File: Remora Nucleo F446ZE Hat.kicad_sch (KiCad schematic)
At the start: 5 parts, among them J1 NucleoF446ZE CN11 Header, J2 NucleoF446ZE CN12 Header

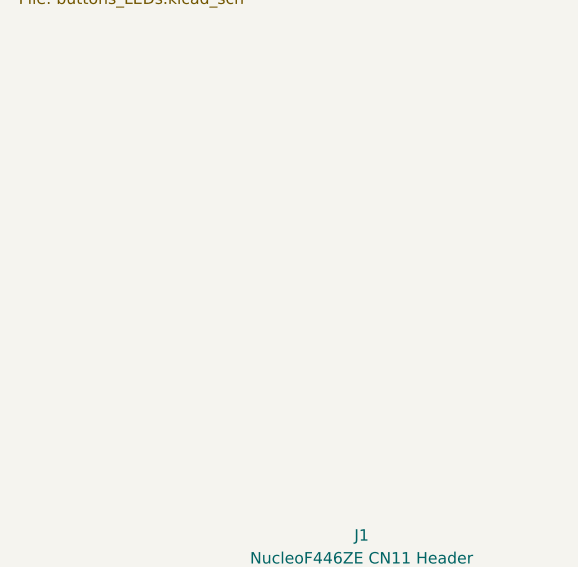
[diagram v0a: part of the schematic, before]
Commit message: tidy of some sheets. Added 0-10V DAC, but untested - only some basic validation on simulator for now
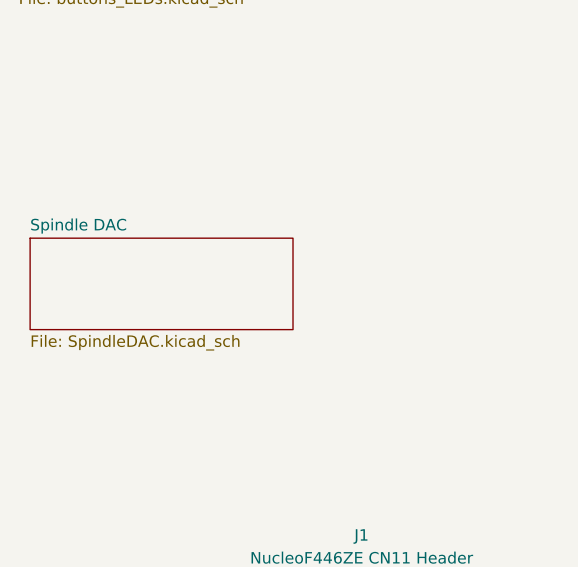
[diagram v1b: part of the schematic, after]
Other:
- added sheet Spindle DAC (SpindleDAC.kicad_sch)
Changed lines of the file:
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@@
+	)
+	(sheet
+		(at 16.51 71.12)
+		(size 29.21 10.16)
+		(exclude_from_sim no)
+		(in_bom yes)
+		(on_board yes)
+		(dnp no)
+		(fields_autoplaced yes)
+		(stroke
+			(width 0.1524)
+			(type solid)
+		)
+		(fill
+			(color 0 0 0 0.0000)
+		)
+		(property "Sheetname" "Spindle DAC"
+			(at 16.51 70.4084 0)
+			(effects
+				(font
+					(size 1.27 1.27)
+				)
+				(justify left bottom)
+			)
+		)
+		(property "Sheetfile" "SpindleDAC.kicad_sch"
+			(at 16.51 81.8646 0)
+			(effects
+				(font
+					(size 1.27 1.27)
+				)
+				(justify left top)
+			)
+		)
+		(instances
+			(project "Remora Nucleo F446ZE Hat"
+				(path "/5473abc6-7b93-43cc-a401-f691c4d7d7cf"
+					(page "18")
+				)
+			)
+		)
 	)
 	(sheet

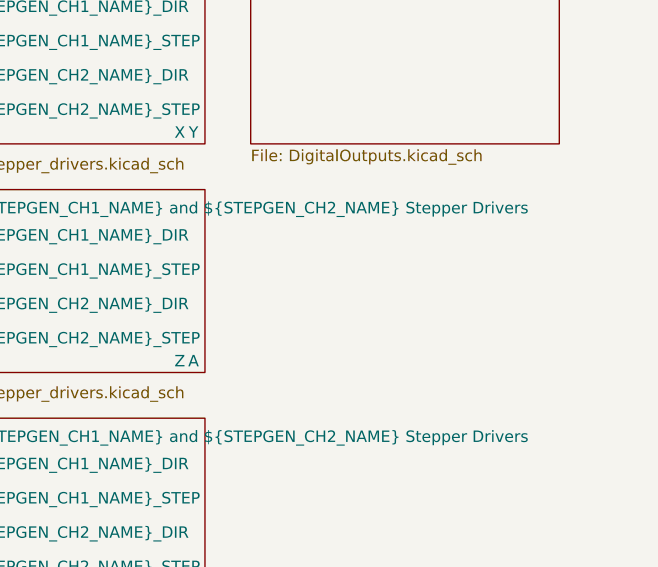
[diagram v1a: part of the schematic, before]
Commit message: digital inputs section
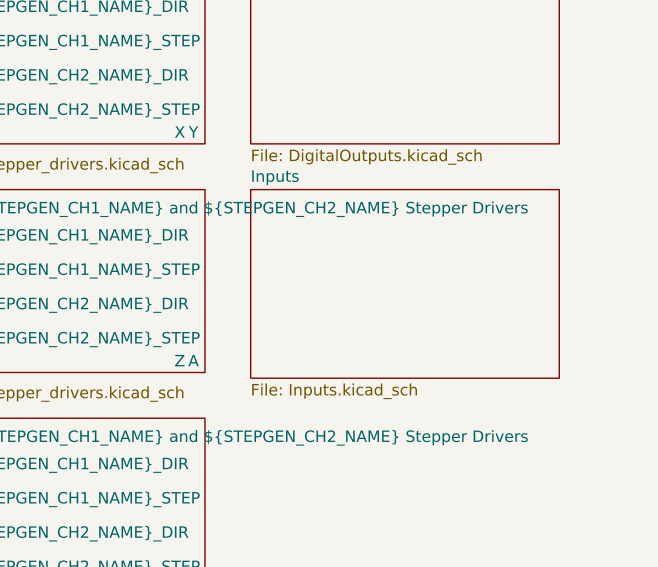
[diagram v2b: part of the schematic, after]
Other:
- added sheet Inputs (Inputs.kicad_sch)
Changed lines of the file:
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@@
+	)
+	(sheet
+		(at 246.38 41.91)
+		(size 34.29 20.955)
+		(exclude_from_sim no)
+		(in_bom yes)
+		(on_board yes)
+		(dnp no)
+		(fields_autoplaced yes)
+		(stroke
+			(width 0.1524)
+			(type solid)
+		)
+		(fill
+			(color 0 0 0 0.0000)
+		)
+		(property "Sheetname" "Inputs"
+			(at 246.38 41.1984 0)
+			(effects
+				(font
+					(size 1.27 1.27)
+				)
+				(justify left bottom)
+			)
+		)
+		(property "Sheetfile" "Inputs.kicad_sch"
+			(at 246.38 63.4496 0)
+			(effects
+				(font
+					(size 1.27 1.27)
+				)
+				(justify left top)
+			)
+		)
+		(instances
+			(project "Remora Nucleo F446ZE Hat"
+				(path "/5473abc6-7b93-43cc-a401-f691c4d7d7cf"
+					(page "19")
+				)
+			)
+		)
 	)
 	(sheet

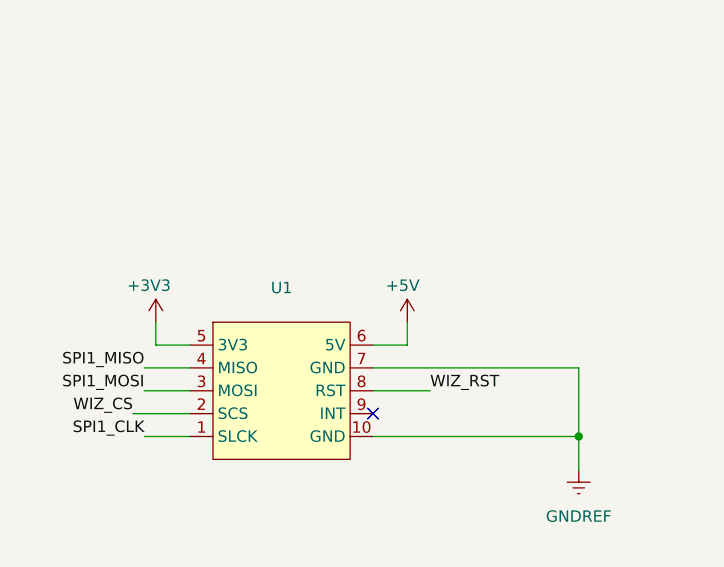
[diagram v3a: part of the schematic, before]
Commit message: restructured power supplies to enable Spindle DAC to be isolated. We now have the option of supplying two 24V inputs, one to power the nucleo and everything logic side and the other to power peripherals. Some testing will be required.
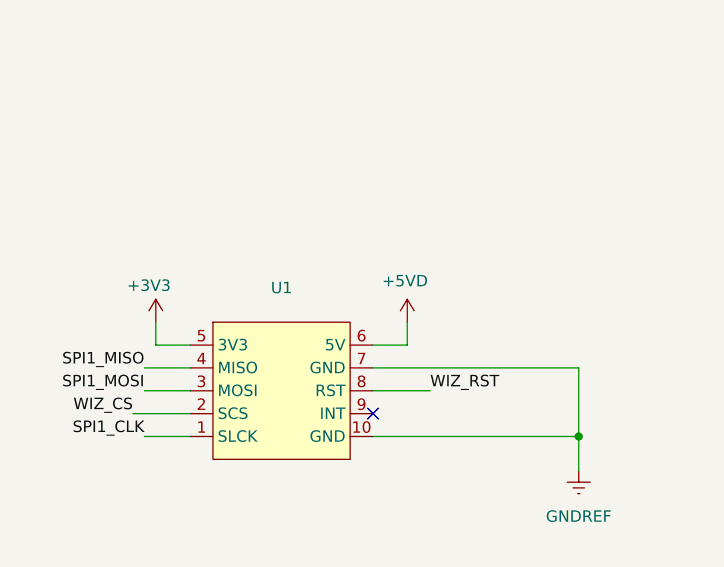
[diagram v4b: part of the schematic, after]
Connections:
- net +5V renamed +5VD
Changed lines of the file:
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@@
+	)
+	(symbol
+		(lib_id "power:+5VD")
+		(at 256.54 140.97 0)
+		(unit 1)
+		(exclude_from_sim no)
+		(in_bom yes)
+		(on_board yes)
+		(dnp no)
+		(property "Reference" "#PWR012"
+			(at 256.54 144.78 0)
+			(effects
+				(font
+					(size 1.27 1.27)
+				)
+				(hide yes)
+			)
+		)
+		(property "Value" "+5VD"
+			(at 256.286 136.398 0)
+			(effects
+				(font
+					(size 1.27 1.27)
+				)
+			)
+		)
+		(property "Footprint" ""
+			(at 256.54 140.97 0)
+			(effects
+				(font
+					(size 1.27 1.27)
+				)
+				(hide yes)
+			)
+		)
+		(property "Datasheet" ""
+			(at 256.54 140.97 0)
+			(effects
+				(font
+					(size 1.27 1.27)
+				)
+				(hide yes)
+			)
+		)
+		(property "Description" "Power symbol creates a global label with name \"+5VD\""
+			(at 256.54 140.97 0)
+			(effects
+				(font
+					(size 1.27 1.27)
+				)
+				(hide yes)
+			)
+		)
+		(pin "1"
+		)
+		(instances
+			(project "Remora Nucleo F446ZE Hat"
+				(path "/5473abc6-7b93-43cc-a401-f691c4d7d7cf"
+					(reference "#PWR012")
+					(unit 1)
+				)
+			)
+		)
 	)
 	(symbol
@@
 					(unit 1)
 				)
-			)
-		)
-	)
-	(symbol
-		(lib_id "power:+5V")
-		(at 256.54 140.97 0)
-		(unit 1)
-		(exclude_from_sim no)
-		(in_bom yes)
-		(on_board yes)
-		(dnp no)
-		(property "Reference" "#PWR012"
-			(at 256.54 144.78 0)
-			(effects
-				(font
-					(size 1.27 1.27)
-				)
-				(hide yes)
-			)
-		)
-		(property "Value" "+5V"
-			(at 256.032 136.906 0)
-			(effects
-				(font
-					(size 1.27 1.27)
-				)
-			)
-		)
-		(property "Footprint" ""
-			(at 256.54 140.97 0)
-			(effects
-				(font
-					(size 1.27 1.27)
-				)
-				(hide yes)
-			)
-		)
-		(property "Datasheet" ""
-			(at 256.54 140.97 0)
-			(effects
-				(font
-					(size 1.27 1.27)
-				)
-				(hide yes)
-			)
-		)
-		(property "Description" "Power symbol creates a global label with name \"+5V\""
-			(at 256.54 140.97 0)
-			(effects
-				(font
-					(size 1.27 1.27)
-				)
-				(hide yes)
-			)
-		)
-		(pin "1"
-		)
-		(instances
-			(project "Remora Nucleo F446RE Hat"
-				(path "/5473abc6-7b93-43cc-a401-f691c4d7d7cf"
-					(reference "#PWR012")
-					(unit 1)
-				)

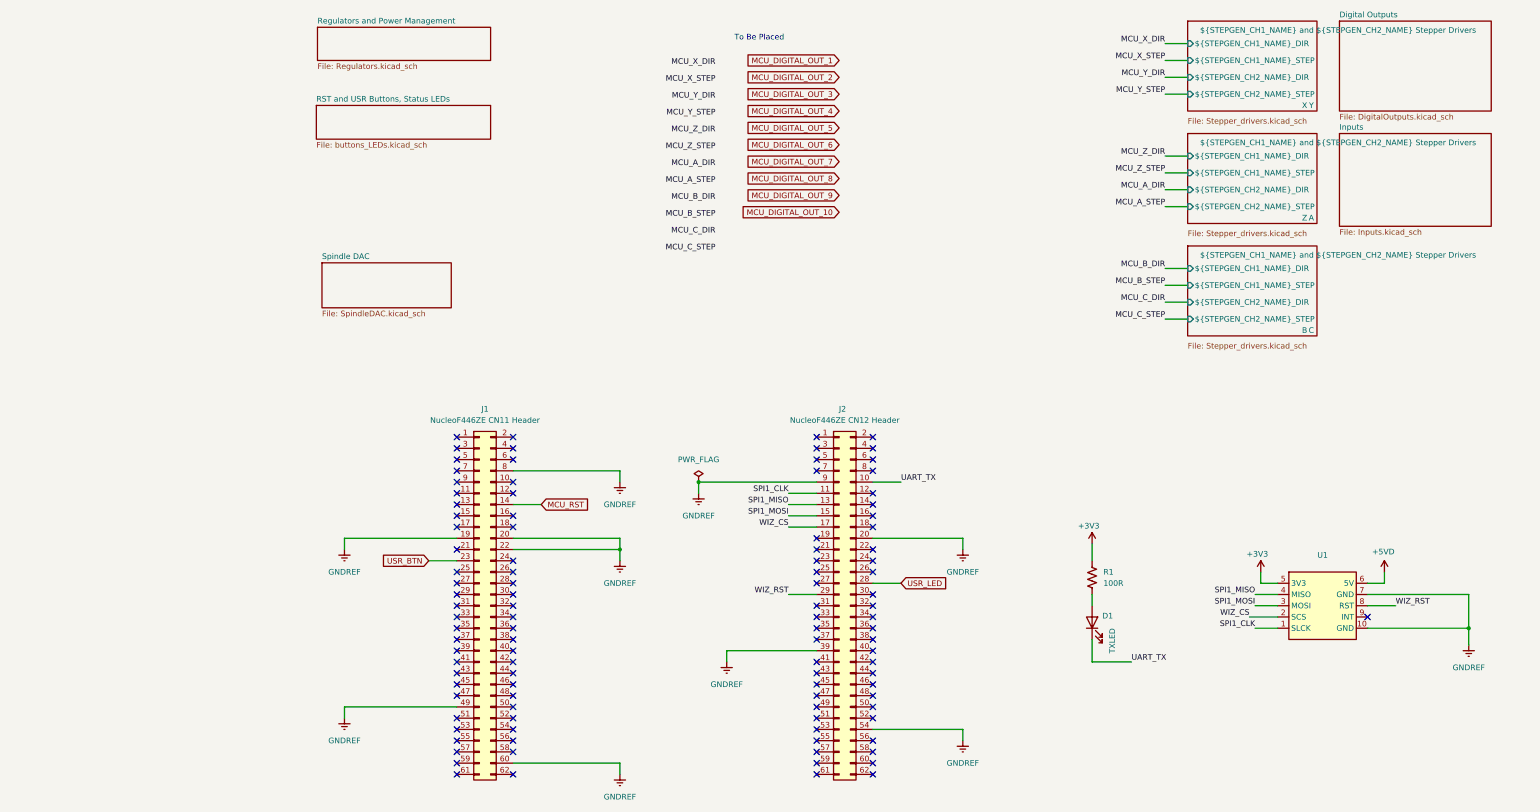
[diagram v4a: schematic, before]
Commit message: moved SPI1_CS to new place. Added MicroSD card and SDIO interface to schematic
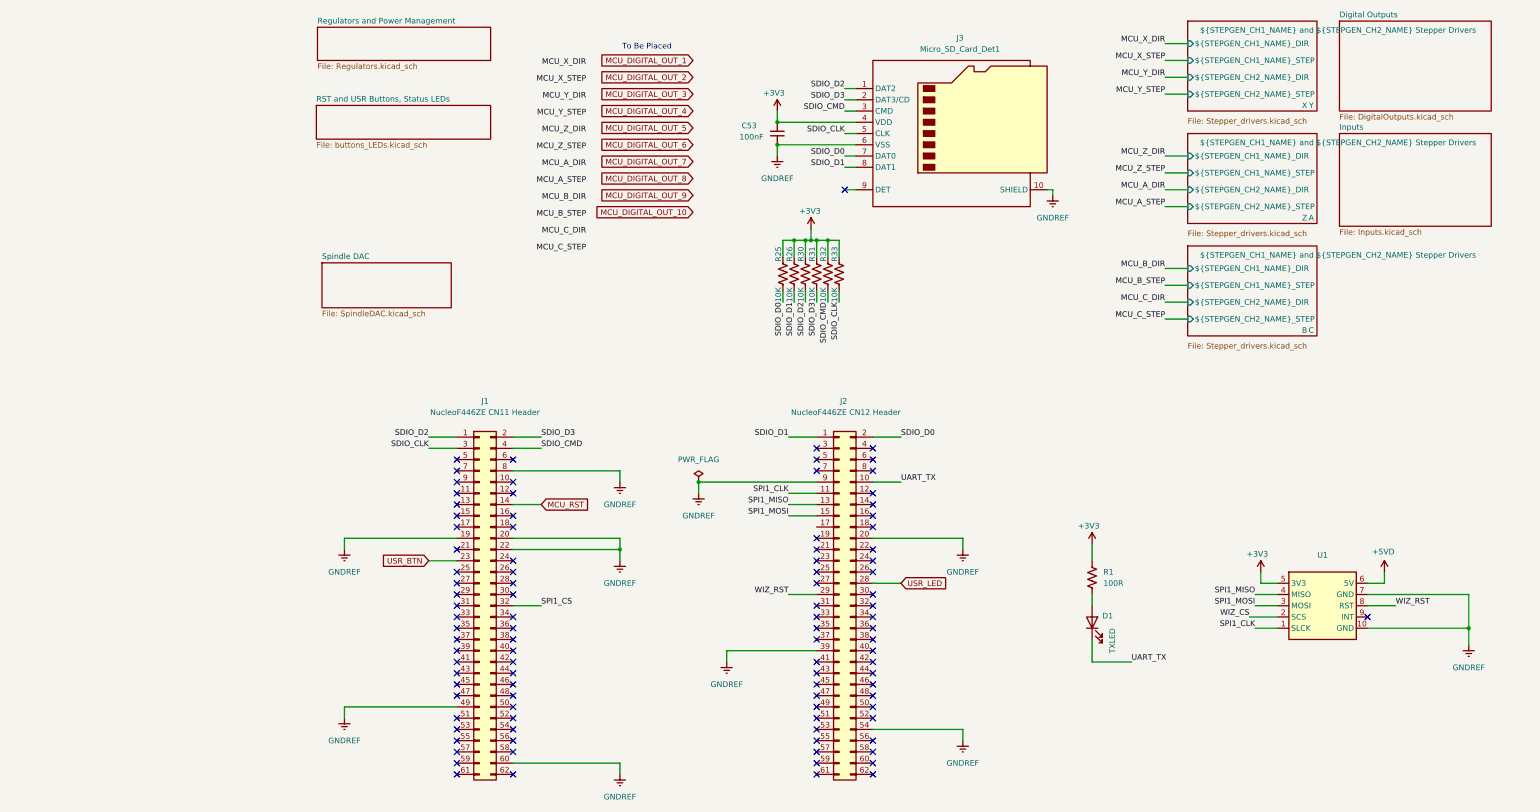
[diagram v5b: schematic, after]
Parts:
- added C53: 100nF, Capacitor_SMD:C_1206_3216Metric_Pad1.33x1.80mm_HandSolder, symbol Device:C_Small
- added J3: Micro_SD_Card_Det1, symbol Connector:Micro_SD_Card_Det1
- added R25, R26, R30, R31, R32, R33: 10K, Resistor_SMD:R_1206_3216Metric_Pad1.30x1.75mm_HandSolder, symbol Device:R_US
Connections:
- net +3V3: now also C53.2, J3.4 (VDD), R25.1, R26.1, R30.1, R31.1, R32.1, R33.1
- net GNDREF: now also C53.1, J3.10 (SHIELD), J3.6 (VSS)
- net WIZ_CS: no longer J2.17 (Pin_17)
- net SDIO_D1: now reaches J2.1 (Pin_1)
- net SDIO_D1: now also J3.8 (DAT1), R26.2
- net SDIO_D0: now reaches J2.2 (Pin_2)
- net SDIO_D0: now also J3.7 (DAT0), R25.2
- net SDIO_D2: now reaches J1.1 (Pin_1)
- net SDIO_D2: now also J3.1 (DAT2), R30.2
- net SDIO_D3: now reaches J1.2 (Pin_2)
- net SDIO_D3: now also J3.2 (DAT3/CD), R31.2
- net SDIO_CLK: now reaches J1.3 (Pin_3)
- net SDIO_CLK: now also J3.5 (CLK), R33.2
- net SPI1_CS: now reaches J1.32 (Pin_32)
- net SDIO_CMD: now reaches J1.4 (Pin_4)
- net SDIO_CMD: now also J3.3 (CMD), R32.2
- no-connect marks 106 -> 100

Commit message: Fixes to bypass caps in micro SD + imported and assigned footprint file
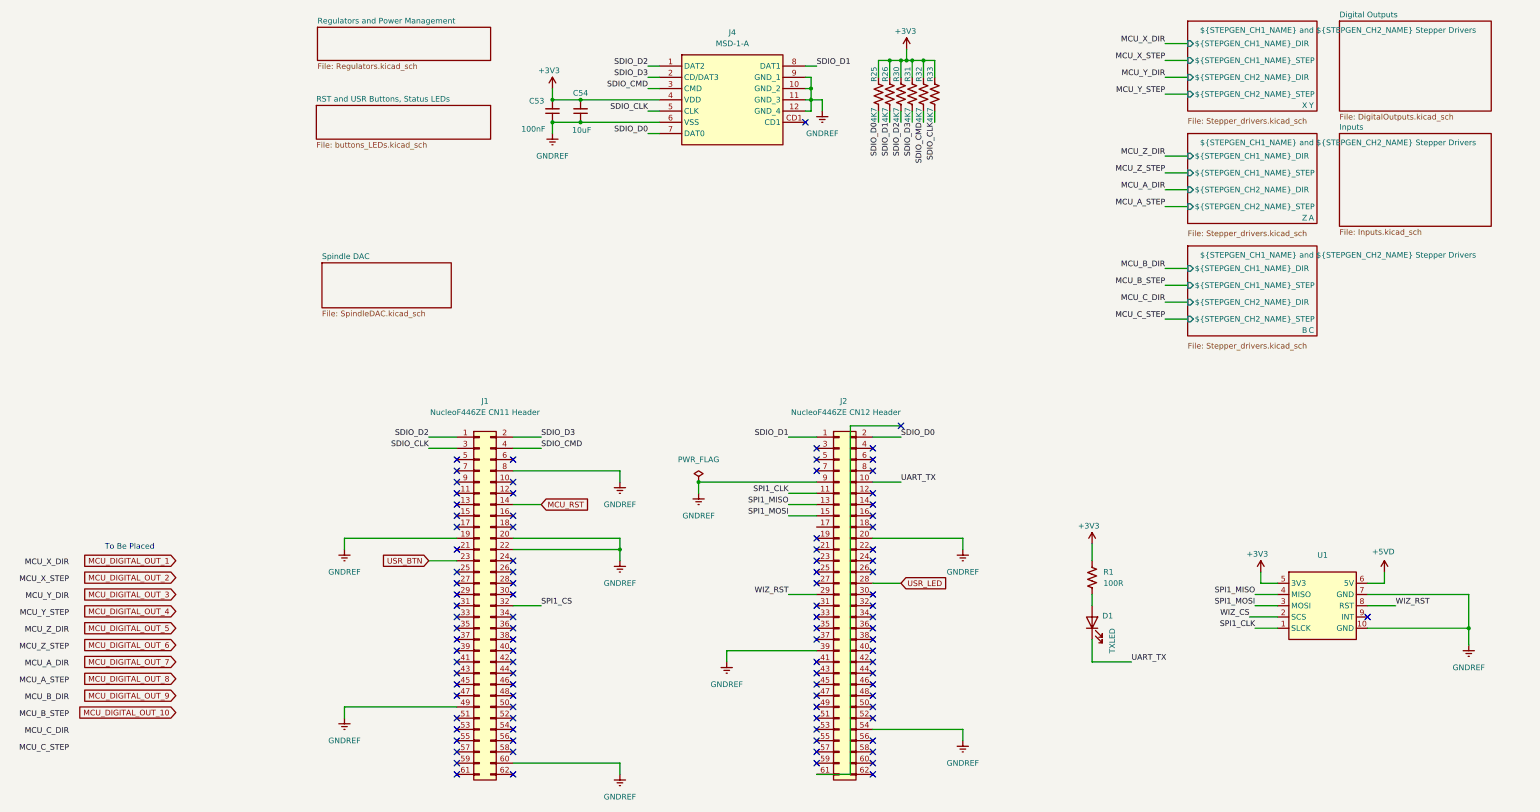
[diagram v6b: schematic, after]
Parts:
- removed J3: Micro_SD_Card_Det1, symbol Connector:Micro_SD_Card_Det1
- added C54: 10uF, Capacitor_SMD:C_1206_3216Metric_Pad1.33x1.80mm_HandSolder, symbol Device:C_Small
- added J4: MSD-1-A, MSD1A Symbols:MSD1A, symbol MSD-1-A:MSD-1-A
- R25, R26, R30, R31, R32, R33: value 10K -> 4K7
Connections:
- net +3V3: now also C54.2, J4.4 (VDD)
- net GNDREF: now also C54.1, J4.10 (GND_2), J4.11 (GND_3), J4.12 (GND_4), J4.6 (VSS), J4.9 (GND_1)
- net SDIO_CLK: now also J4.5 (CLK)
- net SDIO_CMD: now also J4.3 (CMD)
- net SDIO_D0: now also J4.7 (DAT0)
- net SDIO_D1: now also J4.8 (DAT1)
- net SDIO_D2: now also J4.1 (DAT2)
- net SDIO_D3: now also J4.2 (CD/DAT3)
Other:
- moved on the sheet: C53, R25, R26, R30, R31, R32, R33

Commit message: Fixed bug with lack of pin header for CN11 and CN12. Addeded RPI header and aligned it, assigned some safe footprints
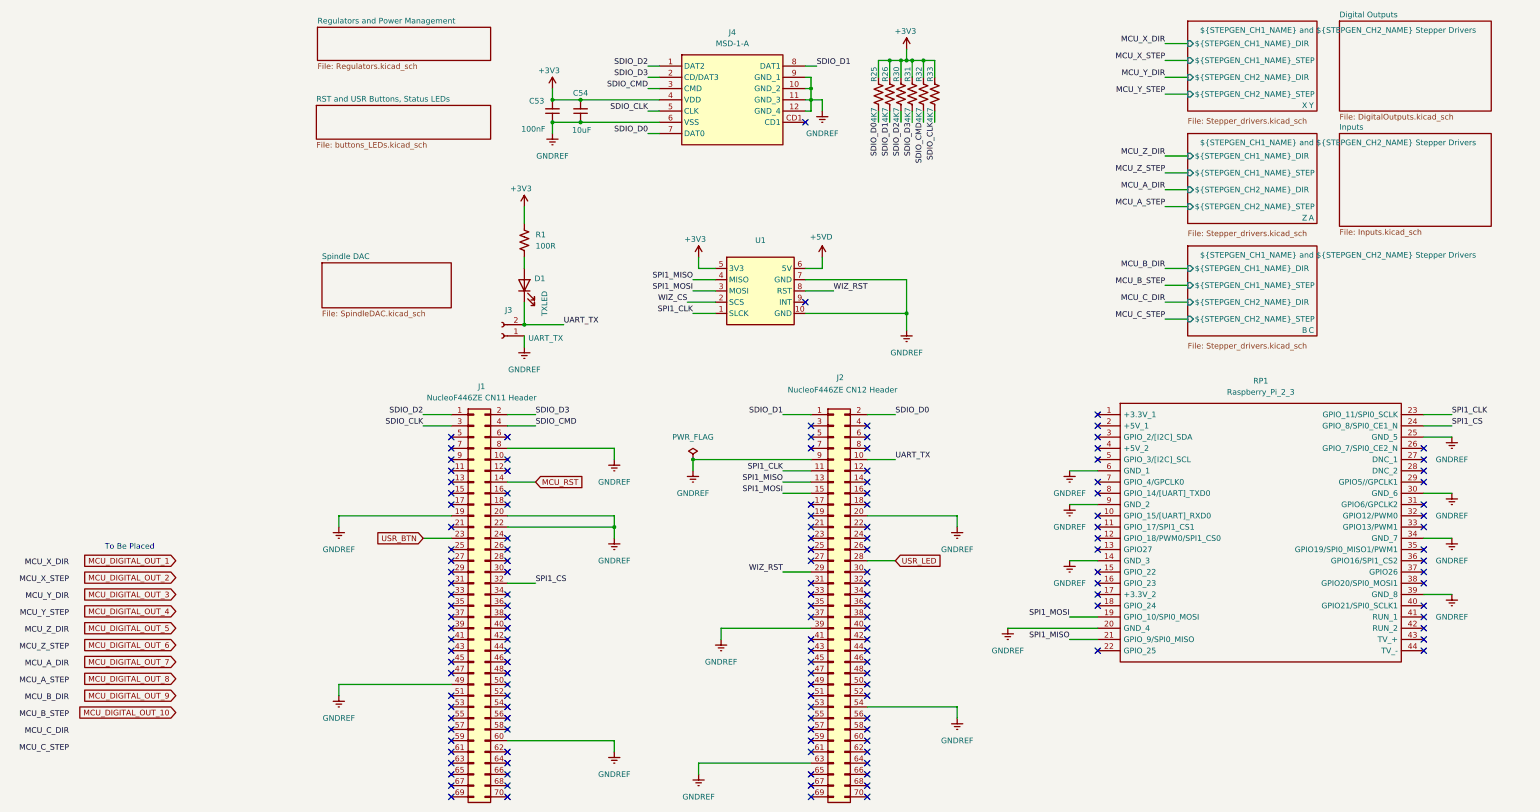
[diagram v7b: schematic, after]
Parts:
- added J3: UART_TX, EBWA_02_A:ADAMTECH_EBWA-02-A, symbol Connector:Conn_01x02_Socket
- added RP1: Raspberry_Pi_2_3, RPI3FootPrint:raspberrypi_2_3, symbol Raspberry_Pi_2_or_3:Raspberry_Pi_2_3
- J1, J2: footprint Connector_PinHeader_2.54mm:PinHeader_2x31_P2.54mm_Vertical -> Connector_PinHeader_2.54mm:PinHeader_2x35_P2.54mm_Vertical; symbol Connector_Generic:Conn_02x31_Odd_Even -> Connector_Generic:Conn_02x35_Odd_Even
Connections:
- net GNDREF: now also J2.63 (Pin_63), J3.1 (Pin_1), RP1.14 (GND_3), RP1.20 (GND_4), RP1.25 (GND_5), RP1.30 (GND_6), RP1.34 (GND_7), RP1.39 (GND_8), RP1.6 (GND_1), RP1.9 (GND_2)
- net SPI1_CLK: now also RP1.23 (GPIO_11/SPI0_SCLK)
- net SPI1_CS: now also RP1.24 (GPIO_8/SPI0_CE1_N)
- net SPI1_MISO: now also RP1.21 (GPIO_9/SPI0_MISO)
- net SPI1_MOSI: now also RP1.19 (GPIO_10/SPI0_MOSI)
- net UART_TX: now also J3.2 (Pin_2)
- no-connect marks 100 -> 148
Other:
- moved on the sheet: D1, R1, U1
